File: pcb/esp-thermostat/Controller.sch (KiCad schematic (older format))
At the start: 25 parts, among them U1 ESP-12F, U2 DS1307Z+, U3 47L04, Y1 Crystal_GND24

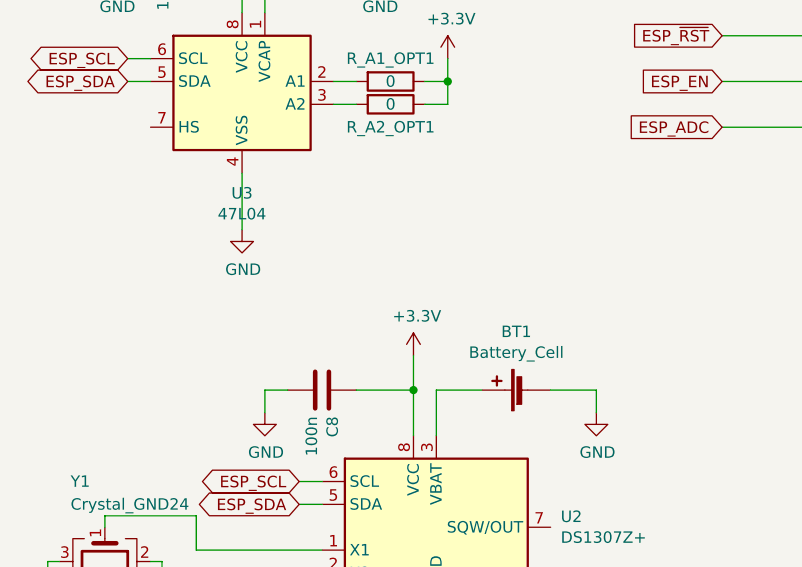
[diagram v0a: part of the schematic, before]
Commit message: PCB: add temp sensor header, optimize routing
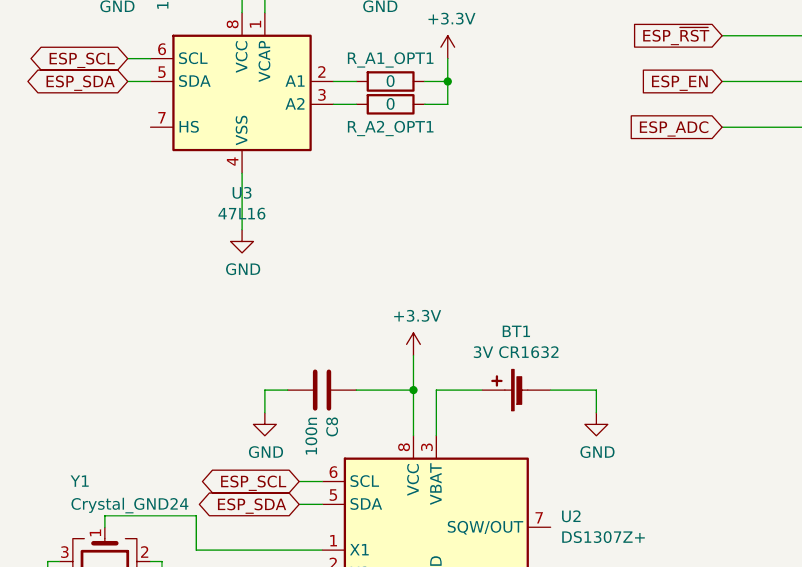
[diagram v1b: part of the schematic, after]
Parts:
- BT1: value Battery_Cell -> 3V CR1632
- U3: value 47L04 -> 47L16
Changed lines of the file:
@@
 EESchema Schematic File Version 4
+LIBS:esp-thermostat-cache
 EELAYER 30 0
 EELAYER END
@@
 P 3150 4850
 F 0 "BT1" V 3405 4900 50  0000 C CNN
-F 1 "Battery_Cell" V 3314 4900 50  0000 C CNN
+F 1 "3V CR1632" V 3314 4900 50  0000 C CNN
 F 2 "Battery:BatteryHolder_CR1632_SMD" V 3150 4910 50  0001 C CNN
 F 3 "~" V 3150 4910 50  0001 C CNN
@@
 P 1900 3500
 F 0 "U3" H 1900 3011 50  0000 C CNN
-F 1 "47L04" H 1900 2920 50  0000 C CNN
+F 1 "47L16" H 1900 2920 50  0000 C CNN
 F 2 "Package_SO:SOIC-8_3.9x4.9mm_P1.27mm" H 1900 3050 50  0001 C CNN
 F 3 "http://ww1.microchip.com/downloads/en/DeviceDoc/20005371C.pdf" H 2150 3850 50  0001 C CNN
